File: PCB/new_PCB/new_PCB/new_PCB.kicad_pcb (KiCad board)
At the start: 2 copper layers, 9 parts, among them U1 ESP32-S3-DEVKITC-1-N16R8V

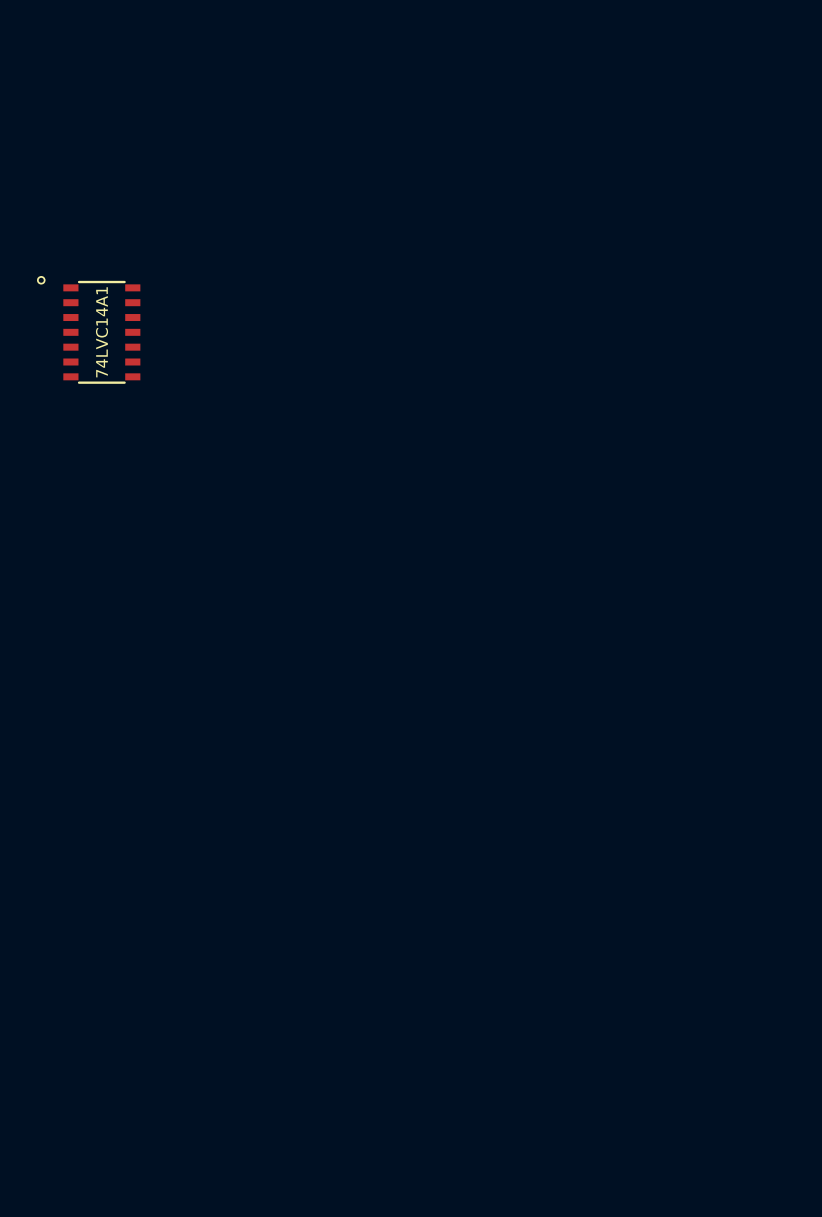
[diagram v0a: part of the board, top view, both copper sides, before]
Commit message: Add servo connectors and 3d models
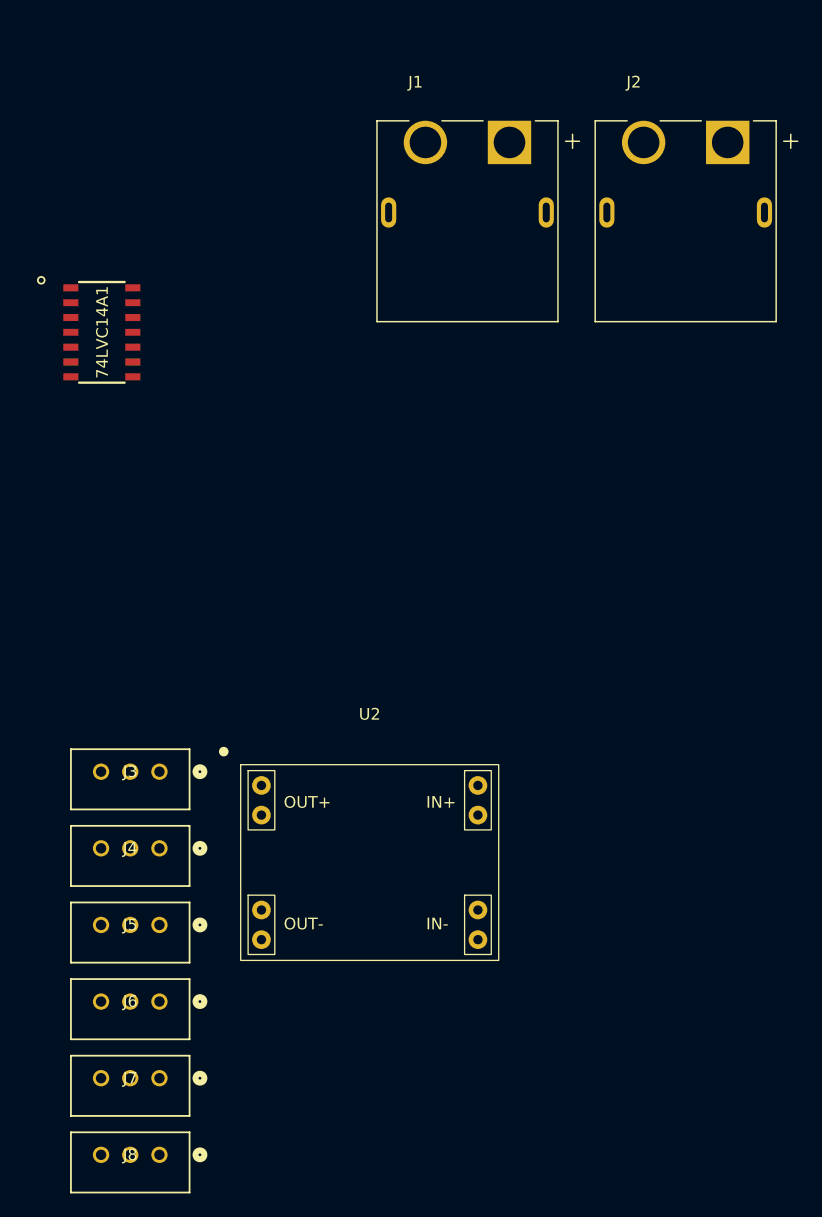
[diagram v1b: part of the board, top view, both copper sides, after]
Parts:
- added J1: XT60PW-F, Elements:AMASS-XT60PW-F, F.Cu at (175.7, 40.2)
- added J2: XT60PW-F, Elements:AMASS-XT60PW-F, F.Cu at (194.4, 40.2)
- added J3: MOLEX-Connector, Elements:CONN_22035035_MOL, F.Cu at (149.3, 94.1)
- added J4: MOLEX-Connector, Elements:CONN_22035035_MOL, F.Cu at (149.3, 100.7)
- added J5: MOLEX-Connector, Elements:CONN_22035035_MOL, F.Cu at (149.3, 107.3)
- added J6: MOLEX-Connector, Elements:CONN_22035035_MOL, F.Cu at (149.3, 113.8)
- added J7: MOLEX-Connector, Elements:CONN_22035035_MOL, F.Cu at (149.3, 120.4)
- added J8: MOLEX-Connector, Elements:CONN_22035035_MOL, F.Cu at (149.3, 126.9)
- added U2: ~, Elements:MP1584EN, F.Cu at (167.3, 101.9)
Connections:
- 74LVC14A1 pad 10: unconnected-(74LVC14A1-5Y-Pad10) -> GND
- 74LVC14A1 pad 11: unconnected-(74LVC14A1-5A-Pad11) -> GND
- 74LVC14A1 pad 12: unconnected-(74LVC14A1-6Y-Pad12) -> GND
- 74LVC14A1 pad 13: unconnected-(74LVC14A1-6A-Pad13) -> GND
- 74LVC14A1 pad 5: unconnected-(74LVC14A1-3A-Pad5) -> GND
- 74LVC14A1 pad 6: unconnected-(74LVC14A1-3Y-Pad6) -> GND
- 74LVC14A1 pad 8: unconnected-(74LVC14A1-4Y-Pad8) -> GND
- 74LVC14A1 pad 9: unconnected-(74LVC14A1-4A-Pad9) -> GND

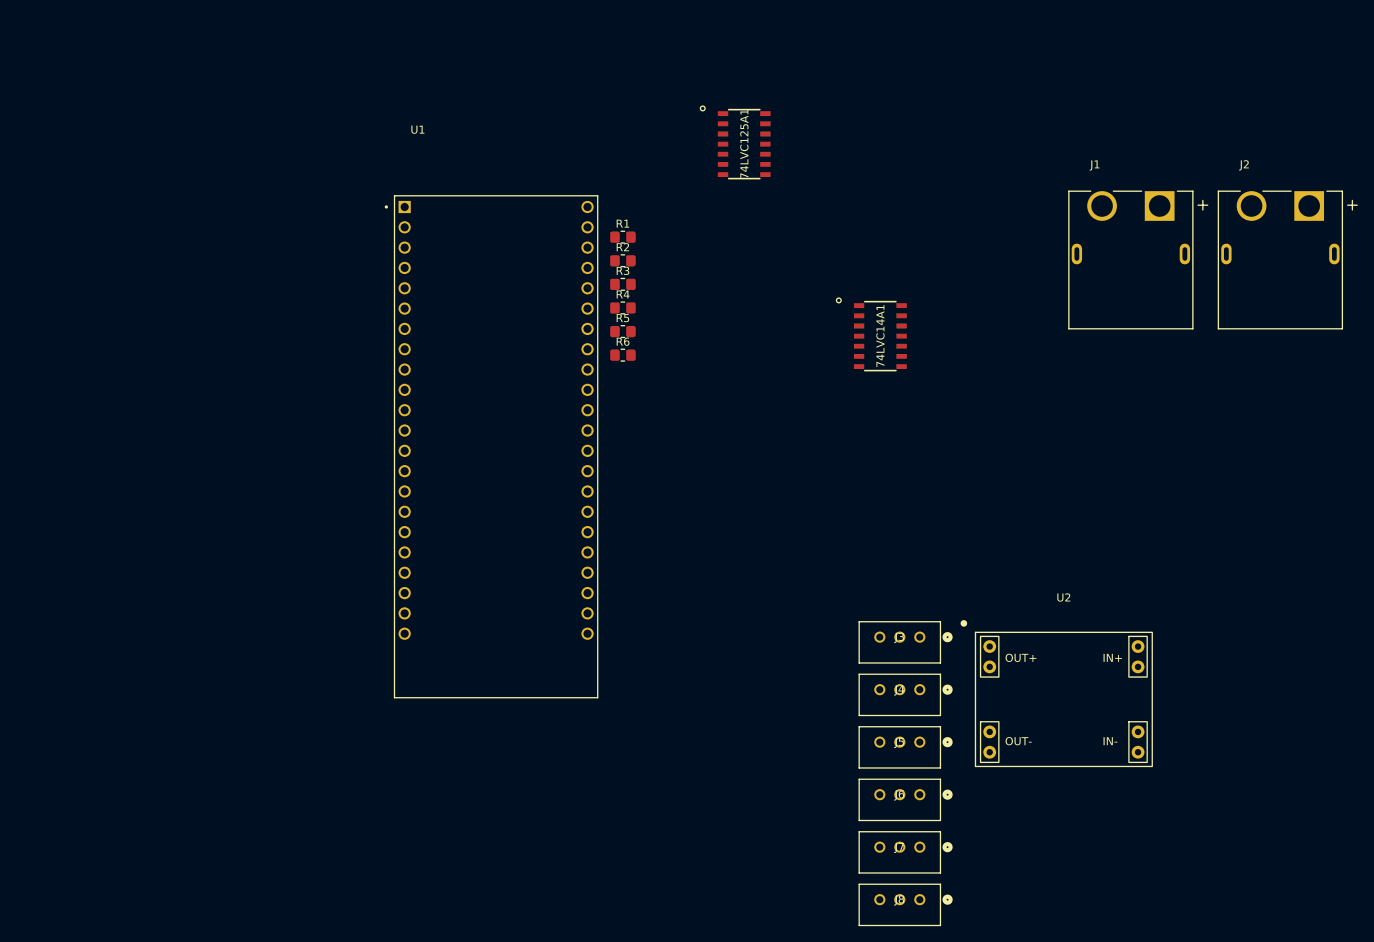
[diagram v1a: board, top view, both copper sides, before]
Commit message: Add first quick version of PCB routing
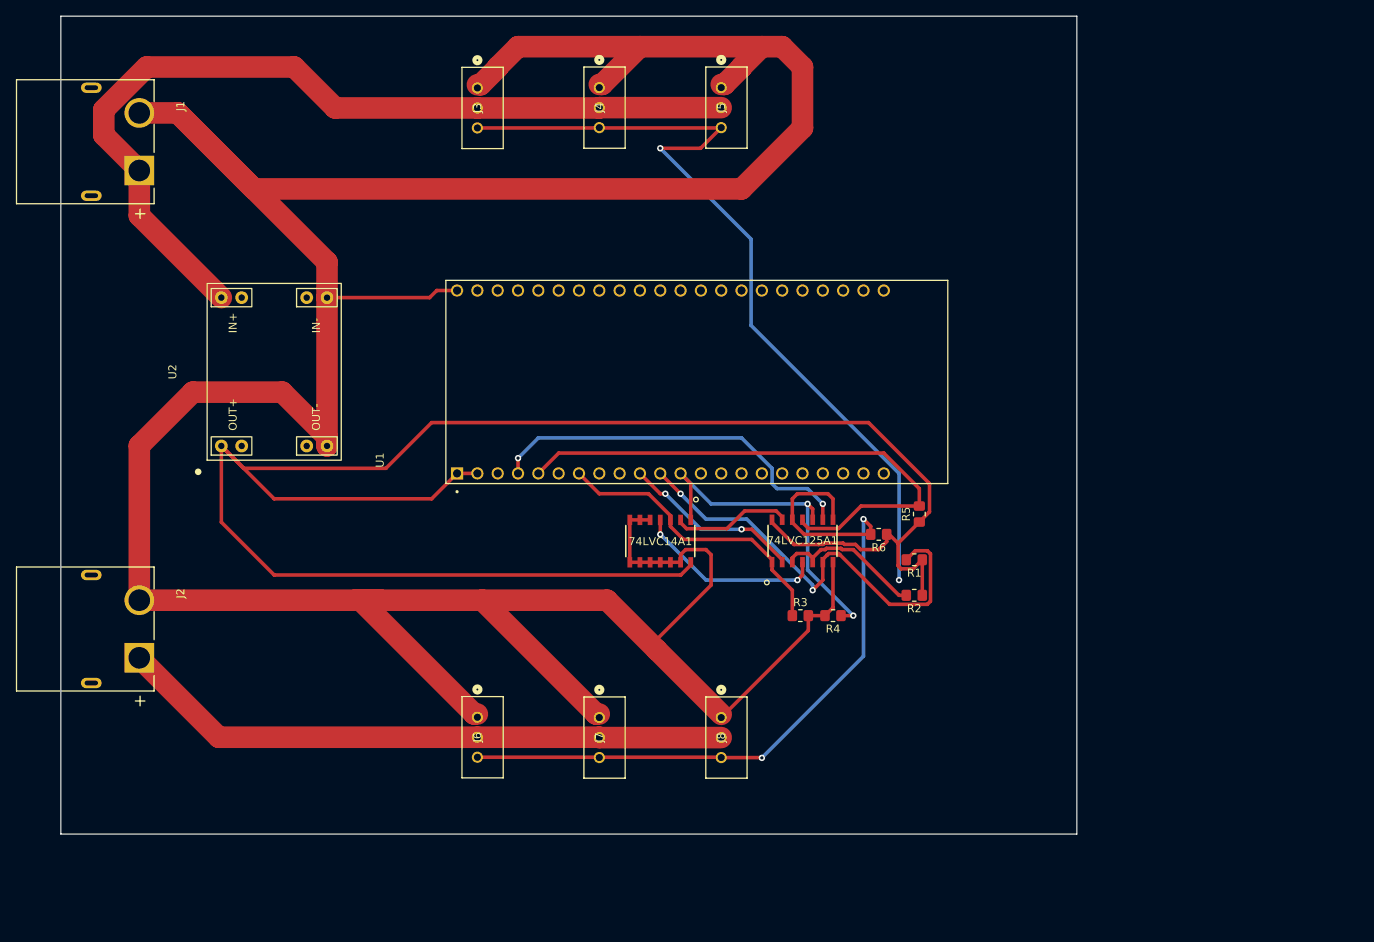
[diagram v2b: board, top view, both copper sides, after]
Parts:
- moved J2 152.1 mm to (51.7, 93.1), turned to -90 degrees
- moved J1 124.2 mm to (51.7, 32.2), turned to -90 degrees
- moved U2 106.9 mm to (68.6, 61.0), turned to 90 degrees
- moved J3 88.2 mm to (94.0, 25.5), turned to 90 degrees
- moved J5 85.5 mm to (124.5, 25.4), turned to 90 degrees
- moved J4 85.3 mm to (109.2, 25.4), turned to 90 degrees
- moved 74LVC125A1 56.4 mm to (130.8, 84.8), turned to 90 degrees
- moved J6 56.1 mm to (94.0, 104.1), turned to 90 degrees
- moved R2 55.5 mm to (148.6, 88.9), turned to 180 degrees
- moved R1 54.3 mm to (148.6, 84.5), turned to 180 degrees
- moved R3 47.0 mm to (134.3, 91.4)
- moved R4 46.6 mm to (138.4, 91.4), turned to 180 degrees
- moved R5 43.5 mm to (149.2, 78.7), turned to 90 degrees
- moved J7 43.2 mm to (109.2, 104.2), turned to 90 degrees
- moved R6 39.0 mm to (144.1, 81.3), turned to 180 degrees
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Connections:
- 74LVC125A1 pad 10: /RXEN1 -> /TXEN2
- 74LVC125A1 pad 4: /TXEN2 -> /RXEN1
- 74LVC125A1 pad 5: /TX2 -> /SERVO_DATA1
- 74LVC125A1 pad 6: /SERVO_DATA2 -> /RX1
- 74LVC125A1 pad 8: /RX1 -> /SERVO_DATA2
- 74LVC125A1 pad 9: /SERVO_DATA1 -> /TX2
- 74LVC14A1 pad 1: /TXEN1 -> /TXEN2
- 74LVC14A1 pad 2: /RXEN1 -> /RXEN2
- 74LVC14A1 pad 3: /TXEN2 -> /TXEN1
- 74LVC14A1 pad 4: /RXEN2 -> /RXEN1
- U1 pad J1_22: GND -> (no net)
- U1 pad J3_21: GND -> (no net)
- U1 pad J3_22: GND -> (no net)
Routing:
- net GND: track 0.00 -> 454.5 mm
- net +3.3V: track 0.00 -> 242.5 mm
- net VBUS: track 0.00 -> 188.0 mm
- net /SERVO_DATA1: track 0.00 -> 124.2 mm, vias 0 -> 2
- net /SERVO_DATA2: track 0.00 -> 94.6 mm, vias 0 -> 2
- net /RX2: track 0.00 -> 69.1 mm
- net /RX1: track 0.00 -> 56.1 mm, vias 0 -> 2
- net /TX2: track 0.00 -> 47.6 mm, vias 0 -> 2
- net /TXEN2: track 0.00 -> 43.9 mm, vias 0 -> 2
- net /TXEN1: track 0.00 -> 37.4 mm
- net /RXEN1: track 0.00 -> 23.8 mm, vias 0 -> 2
- net /TX1: track 0.00 -> 22.5 mm, vias 0 -> 2
- net /RXEN2: track 0.00 -> 14.9 mm
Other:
- board outline added: 127 x 102.2 mm
